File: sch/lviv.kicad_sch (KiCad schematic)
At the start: 0 parts

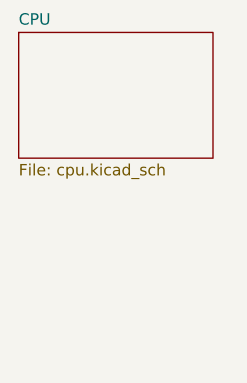
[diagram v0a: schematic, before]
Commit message: Schematic: ROM block
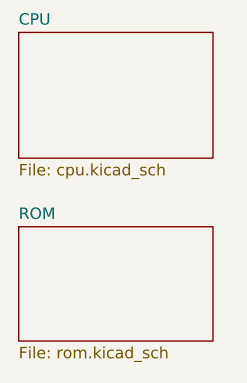
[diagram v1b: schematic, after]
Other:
- added sheet ROM (rom.kicad_sch)
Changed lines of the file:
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@@
 (kicad_sch (version 20211123) (generator eeschema)
   (paper "A4")
+  (sheet (at 44.45 49.53) (size 21.59 12.7) (fields_autoplaced)
+    (stroke (width 0.1524) (type solid) (color 0 0 0 0))
+    (fill (color 0 0 0 0.0000))
+    (property "Sheet name" "ROM" (id 0) (at 44.45 48.8184 0)
+      (effects (font (size 1.27 1.27)) (justify left bottom))
+    )
+    (property "Sheet file" "rom.kicad_sch" (id 1) (at 44.45 62.8146 0)
+      (effects (font (size 1.27 1.27)) (justify left top))
+    )
+  )
   (sheet (at 44.45 27.94) (size 21.59 13.97) (fields_autoplaced)
     (stroke (width 0.1524) (type solid) (color 0 0 0 0))
@@
     (path "/" (page "1"))
     (path "/ec5c2062-3a41-4636-8803-069e60a1641a" (page "2"))
+    (path "/39367e70-4fd8-4578-b7c9-16f6f15e83e4" (page "3"))
   )
   (symbol_instances
@@
       (reference "#PWR?") (unit 1) (value "-5V") (footprint "")
     )
+    (path "/39367e70-4fd8-4578-b7c9-16f6f15e83e4/0a65d90f-0a05-4943-ac2f-92979712c547"
+      (reference "#PWR?") (unit 1) (value "+5V") (footprint "")
+    )
+    (path "/39367e70-4fd8-4578-b7c9-16f6f15e83e4/1238fc37-b0ef-40ea-80c5-a10ab39725c3"
+      (reference "#PWR?") (unit 1) (value "GND") (footprint "")
+    )
     (path "/ec5c2062-3a41-4636-8803-069e60a1641a/2209ee81-6409-4c18-b0f0-f2ebfef5bc4a"
       (reference "#PWR?") (unit 1) (value "+5V") (footprint "")
     )
+    (path "/39367e70-4fd8-4578-b7c9-16f6f15e83e4/2f957223-e1c2-44f7-b013-7319b2fe4e70"
+      (reference "#PWR?") (unit 1) (value "~") (footprint "")
+    )
     (path "/ec5c2062-3a41-4636-8803-069e60a1641a/32e5d193-2867-4d60-9690-db2217d54b19"
       (reference "#PWR?") (unit 1) (value "+5V") (footprint "")
@@
     (path "/ec5c2062-3a41-4636-8803-069e60a1641a/35b51e50-fd32-4078-b7f8-0d2bce36b67c"
       (reference "#PWR?") (unit 1) (value "GND") (footprint "")
+    )
+    (path "/39367e70-4fd8-4578-b7c9-16f6f15e83e4/3fc796d7-53a1-411d-a90c-fa09301d2ae7"
+      (reference "#PWR?") (unit 1) (value "~") (footprint "")
+    )
+    (path "/39367e70-4fd8-4578-b7c9-16f6f15e83e4/401c3817-6d9f-4ce7-8abb-a9eb92c22712"
+      (reference "#PWR?") (unit 1) (value "~") (footprint "")
     )
     (path "/ec5c2062-3a41-4636-8803-069e60a1641a/4190d177-9d65-41f0-a309-2538978aaa9a"
       (reference "#PWR?") (unit 1) (value "+12V") (footprint "")
     )
+    (path "/39367e70-4fd8-4578-b7c9-16f6f15e83e4/4e7eed74-a983-45cb-9e03-b393f9cad20a"
+      (reference "#PWR?") (unit 1) (value "~") (footprint "")
+    )
     (path "/ec5c2062-3a41-4636-8803-069e60a1641a/4f6e87d5-5020-4d60-91cb-aff01d599304"
       (reference "#PWR?") (unit 1) (value "+5V") (footprint "")
     )
+    (path "/39367e70-4fd8-4578-b7c9-16f6f15e83e4/707bb585-cd79-457e-89f5-03f138bb2cb7"
+      (reference "#PWR?") (unit 1) (value "~") (footprint "")
+    )
+    (path "/39367e70-4fd8-4578-b7c9-16f6f15e83e4/7389dbd0-3358-4a90-86bd-d374586f10de"
+      (reference "#PWR?") (unit 1) (value "~") (footprint "")
+    )
+    (path "/39367e70-4fd8-4578-b7c9-16f6f15e83e4/748aacf3-198c-4f1c-82c0-c6bd7fe63b81"
+      (reference "#PWR?") (unit 1) (value "~") (footprint "")
+    )
     (path "/ec5c2062-3a41-4636-8803-069e60a1641a/850ce0f9-8cd8-4855-a5ee-8aeb731b2378"
       (reference "#PWR?") (unit 1) (value "~") (footprint "")
@@
       (reference "#PWR?") (unit 1) (value "GND") (footprint "")
     )
+    (path "/39367e70-4fd8-4578-b7c9-16f6f15e83e4/96e5ac10-1ad3-4a13-94b5-47772c02147c"
+      (reference "#PWR?") (unit 1) (value "+5V") (footprint "")
+    )
+    (path "/39367e70-4fd8-4578-b7c9-16f6f15e83e4/988e80b4-9074-41a7-8fa4-0fb53af0404e"
+      (reference "#PWR?") (unit 1) (value "~") (footprint "")
+    )
+    (path "/39367e70-4fd8-4578-b7c9-16f6f15e83e4/9d823942-46fc-4adc-9ba5-66487a916feb"
+      (reference "#PWR?") (unit 1) (value "~") (footprint "")
+    )
+    (path "/39367e70-4fd8-4578-b7c9-16f6f15e83e4/ac6423a3-531e-4594-b3bd-d11ab6361873"
+      (reference "#PWR?") (unit 1) (value "~") (footprint "")
+    )
     (path "/ec5c2062-3a41-4636-8803-069e60a1641a/b25bf3fc-4b8c-470d-8309-aa0eec2b9625"
       (reference "#PWR?") (unit 1) (value "+5V") (footprint "")
@@
       (reference "#PWR?") (unit 1) (value "+5V") (footprint "")
     )
+    (path "/39367e70-4fd8-4578-b7c9-16f6f15e83e4/c26a68d2-a29a-4992-8792-62929ff7fbe7"
+      (reference "#PWR?") (unit 1) (value "~") (footprint "")
+    )
+    (path "/ec5c2062-3a41-4636-8803-069e60a1641a/c4a3435a-68a1-4d1f-937e-dd4fd074efff"
+      (reference "#PWR?") (unit 1) (value "GND") (footprint "")
+    )
+    (path "/39367e70-4fd8-4578-b7c9-16f6f15e83e4/cfa8b73f-733e-415e-b709-4dc630483904"
+      (reference "#PWR?") (unit 1) (value "GND") (footprint "")
+    )
     (path "/ec5c2062-3a41-4636-8803-069e60a1641a/d4bee014-a77d-4f28-8a6e-bd217537f5f0"
       (reference "#PWR?") (unit 1) (value "+5V") (footprint "")
@@
     (path "/ec5c2062-3a41-4636-8803-069e60a1641a/e30d07a9-ad29-4cbe-a223-85bcb488d3e0"
       (reference "#PWR?") (unit 1) (value "GND") (footprint "")
+    )
+    (path "/39367e70-4fd8-4578-b7c9-16f6f15e83e4/e31a83dd-64d1-4e6c-beb2-757b9ecaa4cb"
+      (reference "#PWR?") (unit 1) (value "+5V") (footprint "")
+    )
+    (path "/39367e70-4fd8-4578-b7c9-16f6f15e83e4/ef6c14c2-90f4-4268-be66-9d8ac087276f"
+      (reference "#PWR?") (unit 1) (value "~") (footprint "")
+    )
+    (path "/39367e70-4fd8-4578-b7c9-16f6f15e83e4/f486d39b-03a2-4981-9e66-2d370c64d806"
+      (reference "#PWR?") (unit 1) (value "~") (footprint "")
+    )
+    (path "/39367e70-4fd8-4578-b7c9-16f6f15e83e4/ff553f31-1684-4de2-8b1b-396c089a5cc2"
+      (reference "#PWR?") (unit 1) (value "~") (footprint "")
     )
     (path "/ec5c2062-3a41-4636-8803-069e60a1641a/463a7f2a-1de0-4b6a-8cee-fc6f4bee1da1"
@@
       (reference "C49") (unit 1) (value "C_Trim") (footprint "")
     )
+    (path "/ec5c2062-3a41-4636-8803-069e60a1641a/a42762ae-33b2-425d-aa2c-10445b69f1d9"
+      (reference "D1") (unit 1) (value "7410") (footprint "")
+    )
+    (path "/ec5c2062-3a41-4636-8803-069e60a1641a/303f88f9-98f1-43d7-bc94-fa291d73b511"
+      (reference "D1") (unit 2) (value "7410") (footprint "")
+    )
     (path "/ec5c2062-3a41-4636-8803-069e60a1641a/caebc74e-3b13-491e-a739-5835ef223ac6"
       (reference "D2") (unit 1) (value "8286 / КР580ВА86") (footprint "")
@@
       (reference "D4") (unit 1) (value "8224 / КР580ГФ24") (footprint "")
     )
+    (path "/ec5c2062-3a41-4636-8803-069e60a1641a/af49318e-88f4-45de-92e0-89cce36323dd"
+      (reference "D5") (unit 1) (value "74LS74") (footprint "")
+    )
     (path "/ec5c2062-3a41-4636-8803-069e60a1641a/becc5b0d-0352-4ad7-ac5e-da033ca0b239"
       (reference "D6") (unit 1) (value "8080 / КР580ВМ80") (footprint "")
     )
+    (path "/ec5c2062-3a41-4636-8803-069e60a1641a/ecb9382e-8212-4cf7-b9a3-cf1f144d2ec8"
+      (reference "D7") (unit 2) (value "7408") (footprint "")
+    )
     (path "/ec5c2062-3a41-4636-8803-069e60a1641a/71507327-aca7-400b-91af-35ed0f809b8f"
       (reference "D8") (unit 1) (value "8228 / КР580ВК28") (footprint "")
     )
+    (path "/39367e70-4fd8-4578-b7c9-16f6f15e83e4/448c97d9-acbf-4cb6-b6cc-530549ead6d1"
+      (reference "D9") (unit 1) (value "74LS138") (footprint "")
+    )
+    (path "/39367e70-4fd8-4578-b7c9-16f6f15e83e4/57b98dec-e562-40c7-93fc-eda6093196c7"
+      (reference "D10") (unit 1) (value "2716") (footprint "")
+    )
+    (path "/39367e70-4fd8-4578-b7c9-16f6f15e83e4/ba9b7247-08b0-43f6-a28f-41d313668186"
+      (reference "D11") (unit 1) (value "~") (footprint "")
+    )
+    (path "/39367e70-4fd8-4578-b7c9-16f6f15e83e4/10eb5a7e-5584-46b0-af38-c6fa2f74b4a0"
+      (reference "D12") (unit 1) (value "~") (footprint "")
+    )
+    (path "/39367e70-4fd8-4578-b7c9-16f6f15e83e4/81f65caf-0943-4d2e-b216-fb25deb75888"
+      (reference "D13") (unit 1) (value "~") (footprint "")
+    )
+    (path "/39367e70-4fd8-4578-b7c9-16f6f15e83e4/31f07217-f6d0-4a14-b3f7-3402d2d3454b"
+      (reference "D14") (unit 1) (value "2716") (footprint "")
+    )
+    (path "/39367e70-4fd8-4578-b7c9-16f6f15e83e4/7dd44cbf-2f1b-4552-8ad1-c8c74a37a4ee"
+      (reference "D15") (unit 1) (value "2716") (footprint "")
+    )
+    (path "/39367e70-4fd8-4578-b7c9-16f6f15e83e4/0bfa49f3-110f-48da-b85d-d99965fc3701"
+      (reference "D16") (unit 1) (value "2716") (footprint "")
+    )
+    (path "/39367e70-4fd8-4578-b7c9-16f6f15e83e4/02303cb1-32c8-4039-8238-ad1a551d64aa"
+      (reference "D17") (unit 1) (value "2716") (footprint "")
+    )
     (path "/ec5c2062-3a41-4636-8803-069e60a1641a/13f7a552-a646-40e6-b51b-e08ee801d2ce"
       (reference "R1") (unit 1) (value "R") (footprint "")
     )
+    (path "/39367e70-4fd8-4578-b7c9-16f6f15e83e4/3f180fb0-8235-45ee-bc3c-db9f3f058fc1"
+      (reference "R2") (unit 1) (value "R") (footprint "")
+    )
     (path "/ec5c2062-3a41-4636-8803-069e60a1641a/1c331ac1-1b0d-406a-87d3-a9df3068fd15"

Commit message: Added RAM block schematic placeholder
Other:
- added sheet RAM (ram.kicad_sch)
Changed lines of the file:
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@@
+    )
+  )
+  (sheet (at 44.45 69.85) (size 21.59 11.43) (fields_autoplaced)
+    (stroke (width 0.1524) (type solid) (color 0 0 0 0))
+    (fill (color 0 0 0 0.0000))
+    (property "Sheet name" "RAM" (id 0) (at 44.45 69.1384 0)
+      (effects (font (size 1.27 1.27)) (justify left bottom))
+    )
+    (property "Sheet file" "ram.kicad_sch" (id 1) (at 44.45 81.8646 0)
+      (effects (font (size 1.27 1.27)) (justify left top))
     )
   )
@@
     (path "/ec5c2062-3a41-4636-8803-069e60a1641a" (page "2"))
     (path "/39367e70-4fd8-4578-b7c9-16f6f15e83e4" (page "3"))
+    (path "/e9506136-80e5-4250-83e4-52799f917e83" (page "4"))
   )
   (symbol_instances

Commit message: Schematic: video part w.i.p.
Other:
- added sheet video (video.kicad_sch)
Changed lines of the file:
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@@
 (kicad_sch (version 20211123) (generator eeschema)
   (paper "A4")
+  (sheet (at 73.66 27.94) (size 21.59 13.97) (fields_autoplaced)
+    (stroke (width 0.1524) (type solid) (color 0 0 0 0))
+    (fill (color 0 0 0 0.0000))
+    (property "Sheet name" "video" (id 0) (at 73.66 27.2284 0)
+      (effects (font (size 1.27 1.27)) (justify left bottom))
+    )
+    (property "Sheet file" "video.kicad_sch" (id 1) (at 73.66 42.4946 0)
+      (effects (font (size 1.27 1.27)) (justify left top))
+    )
+  )
   (sheet (at 44.45 49.53) (size 21.59 12.7) (fields_autoplaced)
     (stroke (width 0.1524) (type solid) (color 0 0 0 0))
@@
     (path "/39367e70-4fd8-4578-b7c9-16f6f15e83e4" (page "3"))
     (path "/e9506136-80e5-4250-83e4-52799f917e83" (page "4"))
+    (path "/036afffe-cbbf-4ead-9c0c-ea4c435dd04c" (page "5"))
   )
   (symbol_instances
@@
       (reference "#PWR?") (unit 1) (value "GND") (footprint "")
     )
+    (path "/036afffe-cbbf-4ead-9c0c-ea4c435dd04c/21a66372-ed48-4a22-a57d-74a4d97cd089"
+      (reference "#PWR?") (unit 1) (value "GND") (footprint "")
+    )
     (path "/ec5c2062-3a41-4636-8803-069e60a1641a/2209ee81-6409-4c18-b0f0-f2ebfef5bc4a"
       (reference "#PWR?") (unit 1) (value "+5V") (footprint "")
+    )
+    (path "/036afffe-cbbf-4ead-9c0c-ea4c435dd04c/2679e4ec-48b4-48bc-95fd-22c4f4834ae1"
+      (reference "#PWR?") (unit 1) (value "GND") (footprint "")
     )
     (path "/39367e70-4fd8-4578-b7c9-16f6f15e83e4/2f957223-e1c2-44f7-b013-7319b2fe4e70"
@@
       (reference "#PWR?") (unit 1) (value "GND") (footprint "")
     )
+    (path "/036afffe-cbbf-4ead-9c0c-ea4c435dd04c/9445c558-efbe-4105-96f5-d1171afc3bbc"
+      (reference "#PWR?") (unit 1) (value "+5V") (footprint "")
+    )
     (path "/39367e70-4fd8-4578-b7c9-16f6f15e83e4/96e5ac10-1ad3-4a13-94b5-47772c02147c"
       (reference "#PWR?") (unit 1) (value "+5V") (footprint "")
@@
       (reference "#PWR?") (unit 1) (value "~") (footprint "")
     )
+    (path "/036afffe-cbbf-4ead-9c0c-ea4c435dd04c/a6748d11-7df4-4581-bd3b-f955d64db32d"
+      (reference "#PWR?") (unit 1) (value "GND") (footprint "")
+    )
     (path "/39367e70-4fd8-4578-b7c9-16f6f15e83e4/ac6423a3-531e-4594-b3bd-d11ab6361873"
       (reference "#PWR?") (unit 1) (value "~") (footprint "")
@@
       (reference "#PWR?") (unit 1) (value "~") (footprint "")
     )
+    (path "/036afffe-cbbf-4ead-9c0c-ea4c435dd04c/f7b6e1a9-c69a-421c-b944-e7350ec4179b"
+      (reference "#PWR?") (unit 1) (value "+5V") (footprint "")
+    )
     (path "/39367e70-4fd8-4578-b7c9-16f6f15e83e4/ff553f31-1684-4de2-8b1b-396c089a5cc2"
       (reference "#PWR?") (unit 1) (value "~") (footprint "")
+    )
+    (path "/036afffe-cbbf-4ead-9c0c-ea4c435dd04c/ffafee13-e17a-4839-ab93-6291ee8cb28e"
+      (reference "#PWR?") (unit 1) (value "+5V") (footprint "")
     )
     (path "/ec5c2062-3a41-4636-8803-069e60a1641a/463a7f2a-1de0-4b6a-8cee-fc6f4bee1da1"
@@
       (reference "C49") (unit 1) (value "C_Trim") (footprint "")
     )
+    (path "/036afffe-cbbf-4ead-9c0c-ea4c435dd04c/b8cf3ca0-43ce-483f-be9e-b1ba17445e31"
+      (reference "C53") (unit 1) (value "~") (footprint "")
+    )
+    (path "/036afffe-cbbf-4ead-9c0c-ea4c435dd04c/5c378429-9b24-44a9-8c23-a863241e2750"
+      (reference "C54") (unit 1) (value "C") (footprint "")
+    )
+    (path "/036afffe-cbbf-4ead-9c0c-ea4c435dd04c/f2073e4f-b840-4d04-8762-43afaffffdaa"
+      (reference "C55") (unit 1) (value "~") (footprint "")
+    )
     (path "/ec5c2062-3a41-4636-8803-069e60a1641a/a42762ae-33b2-425d-aa2c-10445b69f1d9"
       (reference "D1") (unit 1) (value "7410") (footprint "")
@@
       (reference "D17") (unit 1) (value "2716") (footprint "")
     )
+    (path "/036afffe-cbbf-4ead-9c0c-ea4c435dd04c/740ac3f8-0b8d-487f-88b5-1d409ac88bb1"
+      (reference "D29") (unit 1) (value "7401") (footprint "")
+    )
+    (path "/036afffe-cbbf-4ead-9c0c-ea4c435dd04c/6daebe83-aaa4-4961-a38a-cbd8d373aa18"
+      (reference "D29") (unit 2) (value "7401") (footprint "")
+    )
+    (path "/036afffe-cbbf-4ead-9c0c-ea4c435dd04c/027a9fdf-d4cf-4a2f-8554-9eccd8e22f97"
+      (reference "D55") (unit 1) (value "74198") (footprint "")
+    )
+    (path "/036afffe-cbbf-4ead-9c0c-ea4c435dd04c/1e9d0907-eae6-4b87-a782-af578fe9f07d"
+      (reference "D56") (unit 1) (value "74LS155") (footprint "")
+    )
+    (path "/036afffe-cbbf-4ead-9c0c-ea4c435dd04c/b1a7a87d-af24-45d4-89cc-5d2b2cadc156"
+      (reference "D59") (unit 1) (value "7432") (footprint "")
+    )
+    (path "/036afffe-cbbf-4ead-9c0c-ea4c435dd04c/fc3fd5de-c9da-4196-99e9-5704e9cdb305"
+      (reference "D59") (unit 2) (value "7432") (footprint "")
+    )
+    (path "/036afffe-cbbf-4ead-9c0c-ea4c435dd04c/9f4f109a-7719-41d6-8056-6cbe1b40d34e"
+      (reference "D59") (unit 3) (value "7432") (footprint "")
+    )
+    (path "/036afffe-cbbf-4ead-9c0c-ea4c435dd04c/1a9a7ca9-a221-4e29-912f-968e6c98fcb4"
+      (reference "D59") (unit 4) (value "7432") (footprint "")
+    )
+    (path "/036afffe-cbbf-4ead-9c0c-ea4c435dd04c/8cdcf1da-5dcd-4fc6-8073-9a2158952fbf"
+      (reference "D60") (unit 1) (value "7408") (footprint "")
+    )
+    (path "/036afffe-cbbf-4ead-9c0c-ea4c435dd04c/69cbe004-022b-4099-98d4-cde3fa15cc26"
+      (reference "D60") (unit 2) (value "7408") (footprint "")
+    )
+    (path "/036afffe-cbbf-4ead-9c0c-ea4c435dd04c/7911b8cf-4fe8-44ce-a837-20b03c020f6a"
+      (reference "D60") (unit 3) (value "7408") (footprint "")
+    )
+    (path "/036afffe-cbbf-4ead-9c0c-ea4c435dd04c/4cfff88e-f608-47c4-b991-93836701e9ba"
+      (reference "D60") (unit 4) (value "7408") (footprint "")
+    )
+    (path "/036afffe-cbbf-4ead-9c0c-ea4c435dd04c/a16f80ce-37a2-43b6-9ac0-7eff090aad45"
+      (reference "D61") (unit 1) (value "74LS86") (footprint "")
+    )
+    (path "/036afffe-cbbf-4ead-9c0c-ea4c435dd04c/dcc59a2d-0f7e-4a64-a8b5-fe2fd2ce2d5b"
+      (reference "D61") (unit 2) (value "74LS86") (footprint "")
+    )
+    (path "/036afffe-cbbf-4ead-9c0c-ea4c435dd04c/976ef311-2b36-48df-9c6e-b250195ace77"
+      (reference "D61") (unit 3) (value "74LS86") (footprint "")
+    )
+    (path "/036afffe-cbbf-4ead-9c0c-ea4c435dd04c/2d431fb7-30be-46ad-b7f6-8ffc9cb3b140"
+      (reference "D61") (unit 4) (value "74LS86") (footprint "")
+    )
+    (path "/036afffe-cbbf-4ead-9c0c-ea4c435dd04c/69428fcf-c4b7-4246-91ed-cfe5d045b05f"
+      (reference "D62") (unit 1) (value "7432") (footprint "")
+    )
+    (path "/036afffe-cbbf-4ead-9c0c-ea4c435dd04c/03e0db4a-f985-4ff6-bafd-b767f48ef534"
+      (reference "D62") (unit 2) (value "7432") (footprint "")
+    )
+    (path "/036afffe-cbbf-4ead-9c0c-ea4c435dd04c/ea2c0fc1-2833-4b4e-b574-ad2fc842bfc0"
+      (reference "D62") (unit 3) (value "7432") (footprint "")
+    )
+    (path "/036afffe-cbbf-4ead-9c0c-ea4c435dd04c/eed9290e-cdf6-4048-be3f-fef58fd3df7a"
+      (reference "D62") (unit 4) (value "7432") (footprint "")
+    )
     (path "/ec5c2062-3a41-4636-8803-069e60a1641a/13f7a552-a646-40e6-b51b-e08ee801d2ce"
       (reference "R1") (unit 1) (value "R") (footprint "")
@@
       (reference "R2") (unit 1) (value "R") (footprint "")
     )
+    (path "/036afffe-cbbf-4ead-9c0c-ea4c435dd04c/c4f98d67-6592-44c9-8100-d58cc39b8037"
+      (reference "R18") (unit 1) (value "R_Small") (footprint "")
+    )
+    (path "/036afffe-cbbf-4ead-9c0c-ea4c435dd04c/cefd4b1f-1448-4861-84a3-a485ff82a783"
+      (reference "R24") (unit 1) (value "~") (footprint "")
+    )
+    (path "/036afffe-cbbf-4ead-9c0c-ea4c435dd04c/17c99096-a4b6-4c6b-a964-cac597d419f5"
+      (reference "R25") (unit 1) (value "R") (footprint "")
+    )
+    (path "/036afffe-cbbf-4ead-9c0c-ea4c435dd04c/24044c59-3d4e-4f05-a499-5ca759acc8e7"
+      (reference "R26") (unit 1) (value "~") (footprint "")
+    )
+    (path "/036afffe-cbbf-4ead-9c0c-ea4c435dd04c/a265d4f0-e09a-415e-bf35-fd73646a4cc9"
+      (reference "R27") (unit 1) (value "~") (footprint "")
+    )
+    (path "/036afffe-cbbf-4ead-9c0c-ea4c435dd04c/1608ad66-5f05-4083-bd12-920d8a3f372f"
+      (reference "R28") (unit 1) (value "~") (footprint "")
+    )
     (path "/ec5c2062-3a41-4636-8803-069e60a1641a/1c331ac1-1b0d-406a-87d3-a9df3068fd15"
